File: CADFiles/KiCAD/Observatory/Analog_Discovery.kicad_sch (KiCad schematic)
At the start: 1 part, among them J2 Analog Discovery Connection

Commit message: Begin REV 2
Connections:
- net AD_Scope1- is gone; now on net GND: J2.2 (Pin_2)
- net AD_Scope2- is gone; now on net GND: J2.4 (Pin_4)
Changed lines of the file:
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@@
 (kicad_sch
-	(version 20231120)
+	(version 20250114)
 	(generator "eeschema")
-	(generator_version "8.0")
+	(generator_version "9.0")
 	(paper "A4")
+	(junction
+		(at 158.75 81.28)
+		(diameter 0)
+		(color 0 0 0 0)
+	)
+	(junction
+		(at 158.75 86.36)
+		(diameter 0)
+		(color 0 0 0 0)
+	)
+	(junction
+		(at 158.75 83.82)
+		(diameter 0)
+		(color 0 0 0 0)
+	)
 	(wire
 		(pts
-			(xy 134.62 81.28) (xy 138.43 81.28)
+			(xy 134.62 81.28) (xy 158.75 81.28)
 		)
 		(stroke
@@
 	(wire
 		(pts
+			(xy 158.75 81.28) (xy 161.29 81.28)
+		)
+		(stroke
+			(width 0)
+			(type default)
+		)
+	)
+	(wire
+		(pts
 			(xy 134.62 116.84) (xy 138.43 116.84)
 		)
@@
 	(wire
 		(pts
+			(xy 158.75 81.28) (xy 158.75 83.82)
+		)
+		(stroke
+			(width 0)
+			(type default)
+		)
+	)
+	(wire
+		(pts
 			(xy 134.62 88.9) (xy 138.43 88.9)
 		)
@@
 	(wire
 		(pts
+			(xy 158.75 83.82) (xy 161.29 83.82)
+		)
+		(stroke
+			(width 0)
+			(type default)
+		)
+	)
+	(wire
+		(pts
 			(xy 134.62 106.68) (xy 138.43 106.68)
 		)
@@
 	(wire
 		(pts
+			(xy 158.75 83.82) (xy 158.75 86.36)
+		)
+		(stroke
+			(width 0)
+			(type default)
+		)
+	)
+	(wire
+		(pts
 			(xy 134.62 93.98) (xy 154.94 93.98)
 		)
@@
 	(wire
 		(pts
-			(xy 134.62 83.82) (xy 138.43 83.82)
+			(xy 134.62 83.82) (xy 158.75 83.82)
 		)
 		(stroke
@@
 			"uAMAAAAAwEC4AwAAAADAQLgDAAAAAMBAuAMAAAAAwEC4AwAAAADAQLgDAAAAAMBAuAMAAAAAwEC4"
 			"AwAAAADAQLgDAAAAAMBAuAMAAAAAwEC4AwAAAADAQLgDAAAAAMBAuAMAAAAAwEC4AwAAAADAQLgD"
-			"AAAAAMAgjLOiEIv63qMAAAAASUVORK5CYII="
+			"AAAAAMAgjLOiEIv63qMAAAAASUVORK5CYIIAZAAAADEAAAAxAAAAYQAAAGQAAABsAAAAOQAAAFoA"
+			"AABVAAAAMgAAADEAAABPAAAAaAAAAFgAAABrAAAAcgAAAHcAAABPAAAARAAAADQAAABpAAAASwAA"
+			"ACsAAAB1AAAAYwAAAGEAAABqAAAAMAAAAEwAAAAwAAAAZAAAADIAAABJAAAANAAAAFoAAABZAAAA"
+			"YgAAAHkAAABQAAAAcAAAAFAAAABiAAAAawAAADAAAABtAAAAWAAAAGoAAAA2AAAAbwAAAHQAAABT"
+			"AAAAWQAAAFYAAAArAAAAeQAAAEYAAABWAAAAWQAAAHUAAABOAAAAYgAAADgAAABPAAAAOAAAAFgA"
+			"AABWAAAAQgAAADkAAAB0AAAAKwAAAGEAAAAwAAAAdAAAADkAAABkAAAAeAAAAFoAAABqAAAAdAAA"
+			"ADIAAAA2AAAAOQAAAG0AAABUAAAANQAAAG4AAAAvAAAAMwAAAGUAAABtAAAAYgAAACsAAABwAAAA"
+			"eAAAAFUAAAB0AAAATAAAAHUAAAA0AAAAZQAAAHcAAABXAAAAWAAAAEIAAAB5AAAAUwAAAFIAAAB4"
+			"AAAAYgAAAEgAAAB0AAAAQQAAAGMAAABZAAAAegAAADMAAABuAAAAWQAAAFUAAABWAAAAOQAAAHIA"
+			"AABSAAAAaQAAAFUAAABrAAAAaAAAAFcAAABSAAAATgAAAEMAAABMAAAASQAAAGkAAABnAAAAWQAA"
+			"AFEAAABlAAAASQAAAEwAAABmAAAAOQAAADMAAABlAAAARgAAAGQAAABSAAAAawAAAGEAAABaAAAA"
+			"TgAAAEsAAAArAAAAUwAAAGEAAABaAAAAWgAAAHcAAABnAAAAaAAAAGgAAABCAAAAQgAAAEMAAABD"
+			"AAAAQwAAAEgAAABFAAAAQgAAAEEAAAByAAAAdQAAAHMAAAB4AAAAdgAAAHMAAABEAAAAegAAAFcA"
+			"AAA1AAAAQwAAAEEAAAA3AAAATAAAAEsAAABoAAAAOAAAAHkAAAA0AAAATgAAAGMAAABUAAAARQAA"
+			"AFUAAABHAAAAcQAAAHQAAABxAAAAdgAAAE0AAABqAAAAaAAAADIAAAA3AAAATwAAADAAAABWAAAA"
+			"RwAAAFUAAABKAAAAdAAAAFQAAABrAAAAYwAAAFQAAAAxAAAAOQAAAEIAAAB5AAAAeAAAAHEAAABm"
+			"AAAAMgAAAE4AAAB0AAAAUAAAAGQAAABLAAAAWQAAAGYAAAB6AAAAUgAAADIAAAAxAAAAOAAAADYA"
+			"AABFAAAAcQAAAHAAAABnAAAAdgAAAGQAAAByAAAAYwAAAHkAAAByAAAARwAAAGQAAAA3AAAAYgAA"
+			"AEMAAABrAAAATgAAAFAAAAA5AAAAMQAAAA=="
 		)
 	)
@@
 	(global_label "AD_Scope2-"
 		(shape input)
-		(at 138.43 83.82 0)
+		(at 161.29 83.82 0)
 		(fields_autoplaced yes)
 		(effects
@@
 		)
 		(property "Intersheetrefs" "${INTERSHEET_REFS}"
-			(at 153.208 83.82 0)
+			(at 176.068 83.82 0)
 			(effects
 				(font
@@
 	(global_label "AD_Scope1-"
 		(shape input)
-		(at 138.43 81.28 0)
+		(at 161.29 81.28 0)
 		(fields_autoplaced yes)
 		(effects
@@
 		)
 		(property "Intersheetrefs" "${INTERSHEET_REFS}"
-			(at 153.208 81.28 0)
+			(at 176.068 81.28 0)
 			(effects
 				(font

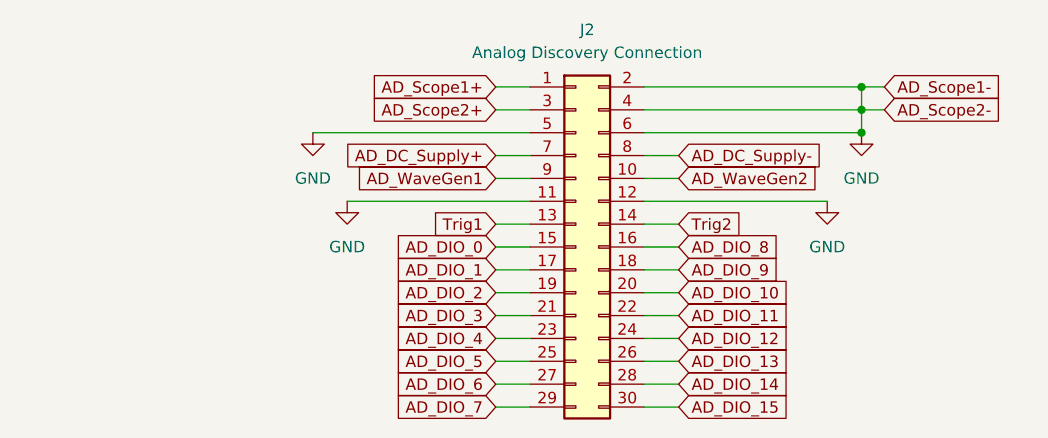
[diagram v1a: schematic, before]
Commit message: All nets routed.
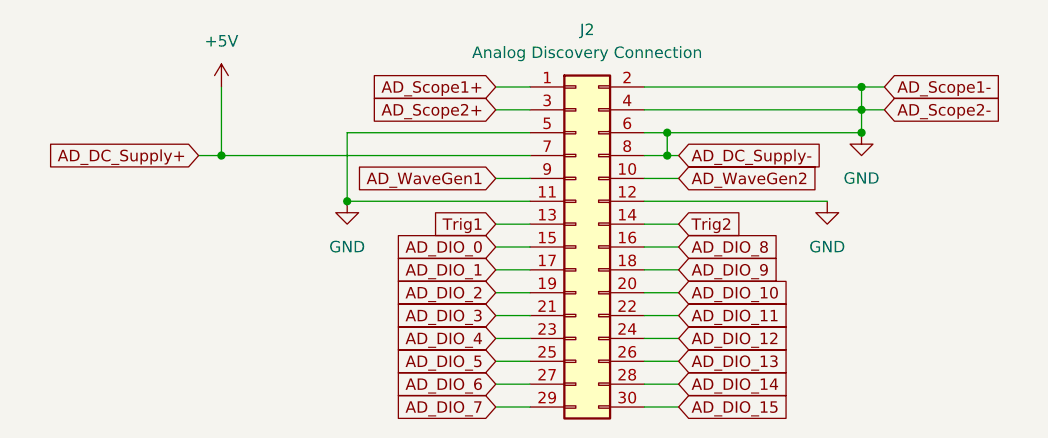
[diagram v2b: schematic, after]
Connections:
- net AD_DC_Supply- is gone; now on net GND: J2.8 (Pin_8)
- net AD_DC_Supply+ renamed +5V

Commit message: AD DC(-) error fixed. Jumpers added for feet grounds and DC supplies
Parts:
- added J25: Jumper, Connector_PinHeader_2.54mm:PinHeader_1x02_P2.54mm_Vertical, symbol Connector:Conn_01x02_Pin
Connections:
- net +5V: now also J25.2 (Pin_2); no longer J2.7 (Pin_7)
- net GND: no longer J2.8 (Pin_8)
- new net: J2.7 (Pin_7), J25.1 (Pin_1)
- new net AD_DC_Supply-: J2.8 (Pin_8)
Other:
- company: (none) -> West Lab
- title: (none) -> SCuM Observatory
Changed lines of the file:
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@@
 	(generator_version "9.0")
 	(paper "A4")
-	(junction
-		(at 137.16 86.36)
-		(diameter 0)
-		(color 0 0 0 0)
-	)
-	(junction
-		(at 137.16 88.9)
-		(diameter 0)
-		(color 0 0 0 0)
+	(title_block
+		(title "SCuM Observatory")
+		(date "2025-03-21")
+		(rev "2")
+		(company "West Lab")
 	)
 	(junction
-		(at 87.63 88.9)
+		(at 158.75 86.36)
 		(diameter 0)
 		(color 0 0 0 0)
@@
 	)
 	(junction
-		(at 158.75 86.36)
-		(diameter 0)
-		(color 0 0 0 0)
-	)
-	(junction
 		(at 158.75 83.82)
 		(diameter 0)
@@
 	(wire
 		(pts
-			(xy 134.62 91.44) (xy 138.43 91.44)
+			(xy 81.28 91.44) (xy 81.28 100.33)
 		)
 		(stroke
@@
 	(wire
 		(pts
-			(xy 118.11 104.14) (xy 121.92 104.14)
+			(xy 83.82 99.06) (xy 83.82 100.33)
 		)
 		(stroke
@@
 	(wire
 		(pts
-			(xy 134.62 111.76) (xy 138.43 111.76)
+			(xy 134.62 91.44) (xy 138.43 91.44)
 		)
 		(stroke
@@
 	(wire
 		(pts
-			(xy 101.6 93.98) (xy 121.92 93.98)
+			(xy 118.11 104.14) (xy 121.92 104.14)
 		)
 		(stroke
@@
 	(wire
 		(pts
-			(xy 158.75 81.28) (xy 158.75 83.82)
+			(xy 134.62 111.76) (xy 138.43 111.76)
 		)
 		(stroke
@@
 	(wire
 		(pts
-			(xy 134.62 88.9) (xy 137.16 88.9)
+			(xy 101.6 93.98) (xy 121.92 93.98)
 		)
 		(stroke
@@
 	(wire
 		(pts
-			(xy 158.75 83.82) (xy 161.29 83.82)
+			(xy 158.75 81.28) (xy 158.75 83.82)
 		)
 		(stroke
@@
 	(wire
 		(pts
-			(xy 134.62 106.68) (xy 138.43 106.68)
+			(xy 158.75 83.82) (xy 161.29 83.82)
 		)
 		(stroke
@@
 	(wire
 		(pts
-			(xy 118.11 83.82) (xy 121.92 83.82)
+			(xy 138.43 88.9) (xy 134.62 88.9)
 		)
 		(stroke
@@
 	(wire
 		(pts
-			(xy 87.63 88.9) (xy 121.92 88.9)
+			(xy 134.62 106.68) (xy 138.43 106.68)
 		)
 		(stroke
@@
 	(wire
 		(pts
-			(xy 137.16 86.36) (xy 137.16 88.9)
+			(xy 118.11 83.82) (xy 121.92 83.82)
 		)
 		(stroke
@@
 	(wire
 		(pts
-			(xy 137.16 86.36) (xy 158.75 86.36)
+			(xy 134.62 86.36) (xy 158.75 86.36)
 		)
 		(stroke
@@
 	(wire
 		(pts
-			(xy 87.63 81.28) (xy 87.63 88.9)
+			(xy 83.82 100.33) (xy 81.28 100.33)
 		)
 		(stroke
@@
 	(wire
 		(pts
-			(xy 134.62 86.36) (xy 137.16 86.36)
+			(xy 81.28 91.44) (xy 77.47 91.44)
 		)
 		(stroke
@@
 	(wire
 		(pts
-			(xy 137.16 88.9) (xy 138.43 88.9)
-		)
-		(stroke
-			(width 0)
-			(type default)
-		)
-	)
-	(wire
-		(pts
 			(xy 118.11 111.76) (xy 121.92 111.76)
 		)
@@
 	(wire
 		(pts
-			(xy 85.09 88.9) (xy 87.63 88.9)
+			(xy 101.6 86.36) (xy 101.6 93.98)
 		)
 		(stroke
@@
 	(wire
 		(pts
-			(xy 101.6 86.36) (xy 101.6 93.98)
+			(xy 118.11 114.3) (xy 121.92 114.3)
 		)
 		(stroke
@@
 	(wire
 		(pts
-			(xy 118.11 114.3) (xy 121.92 114.3)
+			(xy 134.62 83.82) (xy 158.75 83.82)
 		)
 		(stroke
@@
 	(wire
 		(pts
-			(xy 134.62 83.82) (xy 158.75 83.82)
+			(xy 134.62 104.14) (xy 138.43 104.14)
 		)
 		(stroke
@@
 	(wire
 		(pts
-			(xy 134.62 104.14) (xy 138.43 104.14)
+			(xy 77.47 88.9) (xy 121.92 88.9)
 		)
 		(stroke
@@
 			"AFgAAABDAAAANgAAADYAAABkAAAATAAAAFEAAABiAAAAbQAAACsAAAB6AAAARAAAAG8AAAArAAAA"
 			"NwAAAEYAAABVAAAAYwAAADQAAABUAAAAdQAAAEIAAABmAAAAOAAAAE8AAABoAAAANAAAAHYAAABx"
-			"AAAAVwAAAGcAAABJAAAAdAAAADkAAABzAA=="
+			"AAAAVwAAAGcAAABJAAAAdAAAADkAAABzANQOpx6YBQxh1A66epoF6U14Drp6mgWefHgO++qZBYT+"
+			"eA7XtpYFhP54Dnl4kwWefHgOVUSQBQV8dw6cLo0FCwN2DsBKigUJA3YOvUqKBQgDdg67SooF/Rp0"
+			"Dv2qhwXKz3EOyl+FBQwwbw6/d4MFSy1vDld2gwXODW8OTWaDBWNHbg7oqoIFdBZuDlPlgQWMp6kO"
+			"U+WBBYynqQ5QTYQFtR+qDmOphgW4H6oOb6mGBWoLqw524ogFcQurDoPiiAWiYawOouKKBaVhrA6m"
+			"4ooFKxWuDiyWjAUvFa4OL5aMBU4VsA5g7I0FWxWwDmfsjQViTrIOGdiOBWdOsg4b2I4FbcOzDk4i"
+			"jwWBqrQORVCPBYSqtA5GUI8Fhqq0DkZQjwV8ErcORlCPBX0Stw5FUI8FmW65DhvYjgWrp7sOZOyN"
+			"BdGnvQ4vlowFXVu/DqPiigWSscAOfeKIBUmdwQ5rqYYFdBXCDkxNhAV0FcIOWOWBBXQVwg5V5YEF"
+			"cxXCDlPlgQW++8EOFWSBBUmdwQ45iX8FBZTBDttyfwWVscAOLVB9BY6xwA4gUH0FXVu/DgFQewVa"
+			"W78O/U97BdSnvQ53nHkF0Ke9DnSceQVY2LsOxWZ4BSxs9A7FZngFLGz0DsLOegVV5PQO1Sp9BVjk"
+			"9A7hKn0FCtD1DuhjfwUR0PUO9WN/BUIm9w4UZIEFRSb3DhhkgQXL2fgOnheDBc/Z+A6hF4MF7tn6"
+			"DtJthAX72foO2W2EBe00/A6O/YQFBxP9Do1ZhQUhb/8Ot9GFBSRv/w640YUFJm//DrjRhQUc1wEP"
+			"uNGFBR3XAQ+30YUFOTMED41ZhQVLbAYP1m2EBXFsCA+hF4MF/R8KDxVkgQUydgsP72N/BelhDA/d"
+			"Kn0FFNoMD77OegUU2gwPymZ4BRTaDA/HZngFE9oMD8VmeAUWtAwPzKd3BelhDA+rCnYF52EMD6YK"
+			"dgU1dgsPn9FzBS52Cw+S0XMF/R8KD3PRcQX6HwoPb9FxBXRsCA/pHXAFcGwID+YdcAVRbAYPtcdu"
+			"BURsBg+ux24FPTMED/zbbQUxMwQP+dttBR3XAQ/QY20FGtcBD9BjbQUmb/8O0GNtBSNv/w7QY20F"
+			"DhP9DvnbbQUCE/0O/NttBfvZ+g6ux24F7tn6DrXHbgXP2fgO5h1wBcvZ+A7pHXAFRSb3Dm/RcQVC"
+			"JvcOc9FxBRHQ9Q6S0XMFCtD1Dp/RcwVY5PQOpgp2BVXk9A6yCnYFLGz0DsVmeAVY2LsOxWZ4BbGn"
+			"uw5DRngFpKe7DjxGeAWdbrkOilp3BZFuuQ6HWncFfRK3Dl7idgV6ErcOXuJ2BYaqtA5e4nYFg6q0"
+			"Dl7idgVuTrIOh1p3BWJOsg6KWncFWxWwDg=="
 		)
 	)
@@
 		)
 	)
+	(global_label "AD_DC_Supply-"
+		(shape input)
+		(at 138.43 88.9 0)
+		(fields_autoplaced yes)
+		(effects
+			(font
+				(size 1.27 1.27)
+			)
+			(justify left)
+		)
+		(property "Intersheetrefs" "${INTERSHEET_REFS}"
+			(at 156.1107 88.9 0)
+			(effects
+				(font
+					(size 1.27 1.27)
+				)
+				(justify left)
+				(hide yes)
+			)
+		)
+	)
 	(global_label "AD_Scope2+"
 		(shape input)
@@
 		)
 	)
-	(global_label "AD_DC_Supply+"
-		(shape input)
-		(at 85.09 88.9 180)
-		(fields_autoplaced yes)
-		(effects
-			(font
-				(size 1.27 1.27)
-			)
-			(justify right)
-		)
-		(property "Intersheetrefs" "${INTERSHEET_REFS}"
-			(at 67.4093 88.9 0)
-			(effects
-				(font
-					(size 1.27 1.27)
-				)
-				(justify right)
-				(hide yes)
-			)
-		)
-	)
 	(global_label "AD_DIO_1"
 		(shape input)
@@
 		)
 	)
-	(global_label "AD_DC_Supply-"
-		(shape input)
-		(at 138.43 88.9 0)
-		(fields_autoplaced yes)
-		(effects
-			(font
-				(size 1.27 1.27)
-			)
-			(justify left)
-		)
-		(property "Intersheetrefs" "${INTERSHEET_REFS}"
-			(at 156.1107 88.9 0)
-			(effects
-				(font
-					(size 1.27 1.27)
-				)
-				(justify left)
-				(hide yes)
-			)
-		)
-	)
 	(global_label "AD_Scope2-"
 		(shape input)
@@
 		(dnp no)
 		(fields_autoplaced yes)
-		(property "Reference" "#PWR06"
+		(property "Reference" "#PWR038"
 			(at 158.75 92.71 0)
 			(effects
@@
 		)
 		(instances
+			(project "Observatory"
+				(path "/70f40ce9-32c8-42da-85f6-43c2f6e1fb63/8524221f-2795-4c43-bbcc-559842e72345"
+					(reference "#PWR038")
+					(unit 1)
+				)
+			)
+		)
+	)
+	(symbol
+		(lib_id "Connector:Conn_01x02_Pin")
+		(at 72.39 88.9 0)
+		(unit 1)
+		(exclude_from_sim no)
+		(in_bom yes)
+		(on_board yes)
+		(dnp no)
+		(fields_autoplaced yes)
+		(property "Reference" "J25"
+			(at 73.025 83.82 0)
+			(effects
+				(font
+					(size 1.27 1.27)
+				)
+			)
+		)
+		(property "Value" "Jumper"
+			(at 73.025 86.36 0)
+			(effects
+				(font
+					(size 1.27 1.27)
+				)
+			)
+		)
+		(property "Footprint" "Connector_PinHeader_2.54mm:PinHeader_1x02_P2.54mm_Vertical"
+			(at 72.39 88.9 0)
+			(effects
+				(font
+					(size 1.27 1.27)
+				)
+				(hide yes)
+			)
+		)
+		(property "Datasheet" "~"
+			(at 72.39 88.9 0)
+			(effects
+				(font
+					(size 1.27 1.27)
+				)
+				(hide yes)
+			)
+		)
+		(property "Description" "Generic connector, single row, 01x02, script generated"
+			(at 72.39 88.9 0)
+			(effects
+				(font
+					(size 1.27 1.27)
+				)
+				(hide yes)
+			)
+		)
+		(pin "2"
+		)
+		(pin "1"
+		)
+		(instances
 			(project ""
 				(path "/70f40ce9-32c8-42da-85f6-43c2f6e1fb63/8524221f-2795-4c43-bbcc-559842e72345"
-					(reference "#PWR06")
+					(reference "J25")
 					(unit 1)
 				)
@@
 	(symbol
 		(lib_id "power:+5V")
-		(at 87.63 81.28 0)
+		(at 83.82 99.06 0)
 		(unit 1)
 		(exclude_from_sim no)
@@
 		(fields_autoplaced yes)
 		(property "Reference" "#PWR037"
-			(at 87.63 85.09 0)
+			(at 83.82 102.87 0)
 			(effects
 				(font
@@
 		)
 		(property "Value" "+5V"
-			(at 87.63 76.2 0)
+			(at 83.82 93.98 0)
 			(effects
 				(font
@@
 		)
 		(property "Footprint" ""
-			(at 87.63 81.28 0)
+			(at 83.82 99.06 0)
 			(effects
 				(font
@@
 		)
 		(property "Datasheet" ""
-			(at 87.63 81.28 0)
+			(at 83.82 99.06 0)
 			(effects
 				(font
@@
 		)
 		(property "Description" "Power symbol creates a global label with name \"+5V\""
-			(at 87.63 81.28 0)
+			(at 83.82 99.06 0)
 			(effects
 				(font
